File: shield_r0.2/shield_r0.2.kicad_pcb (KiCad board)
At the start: 2 copper layers, 124.5 x 55.9 mm, 10 parts, among them X6 X6, X7 X7, X8 X8, X9 X9

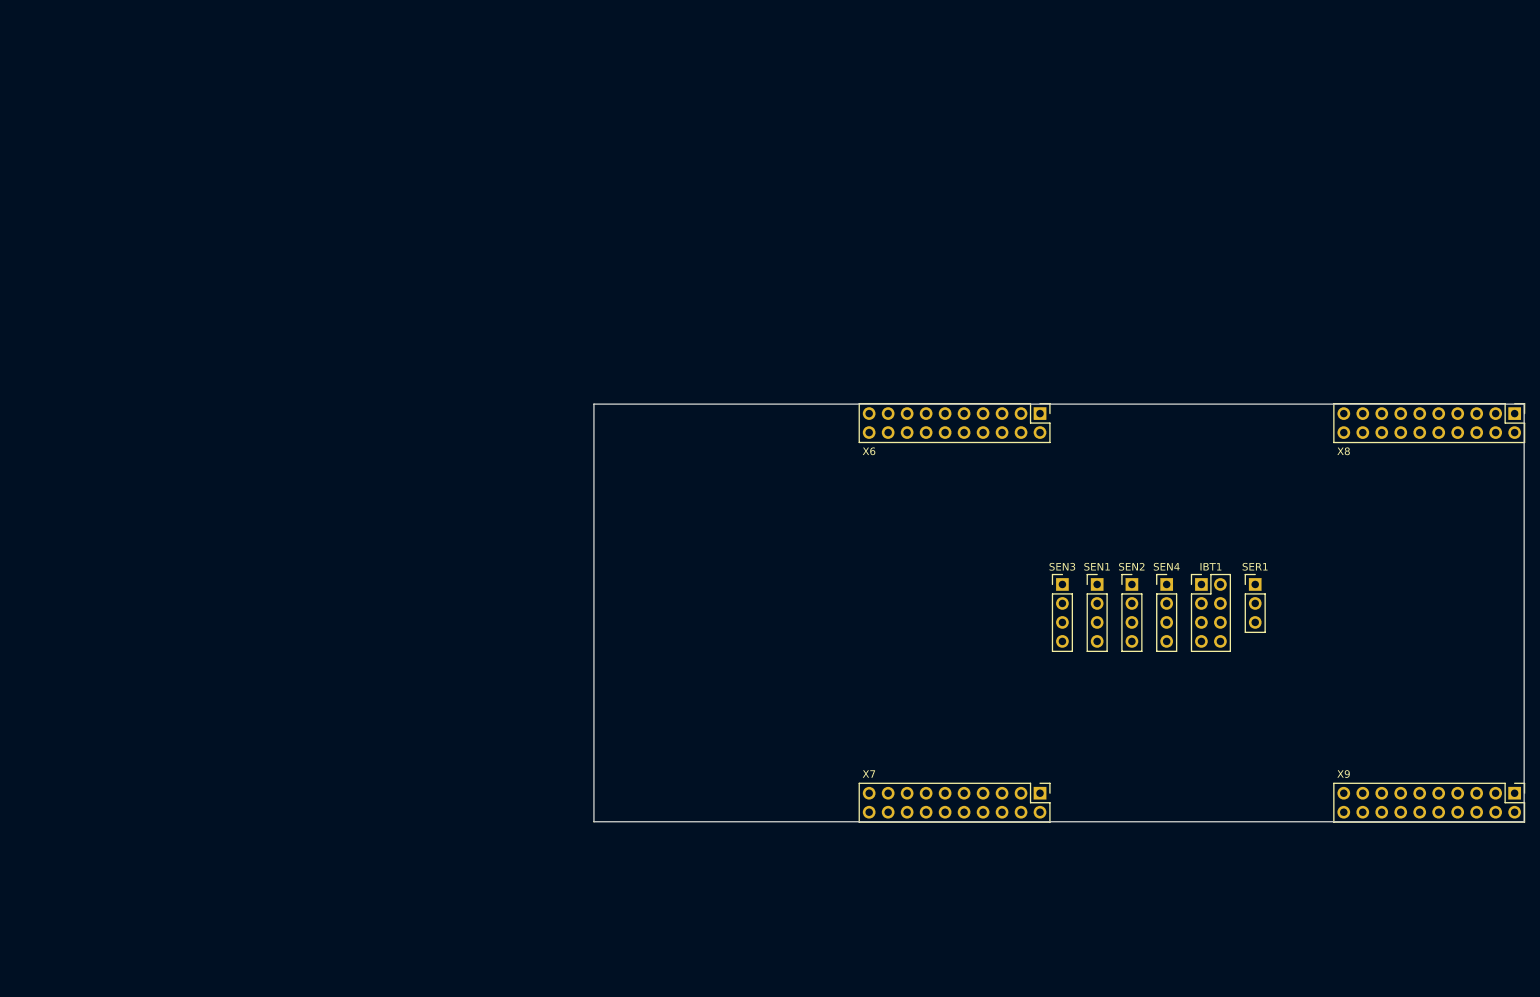
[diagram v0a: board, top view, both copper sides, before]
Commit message: crear librerías ibt-2 y tiva-c, muestra shield
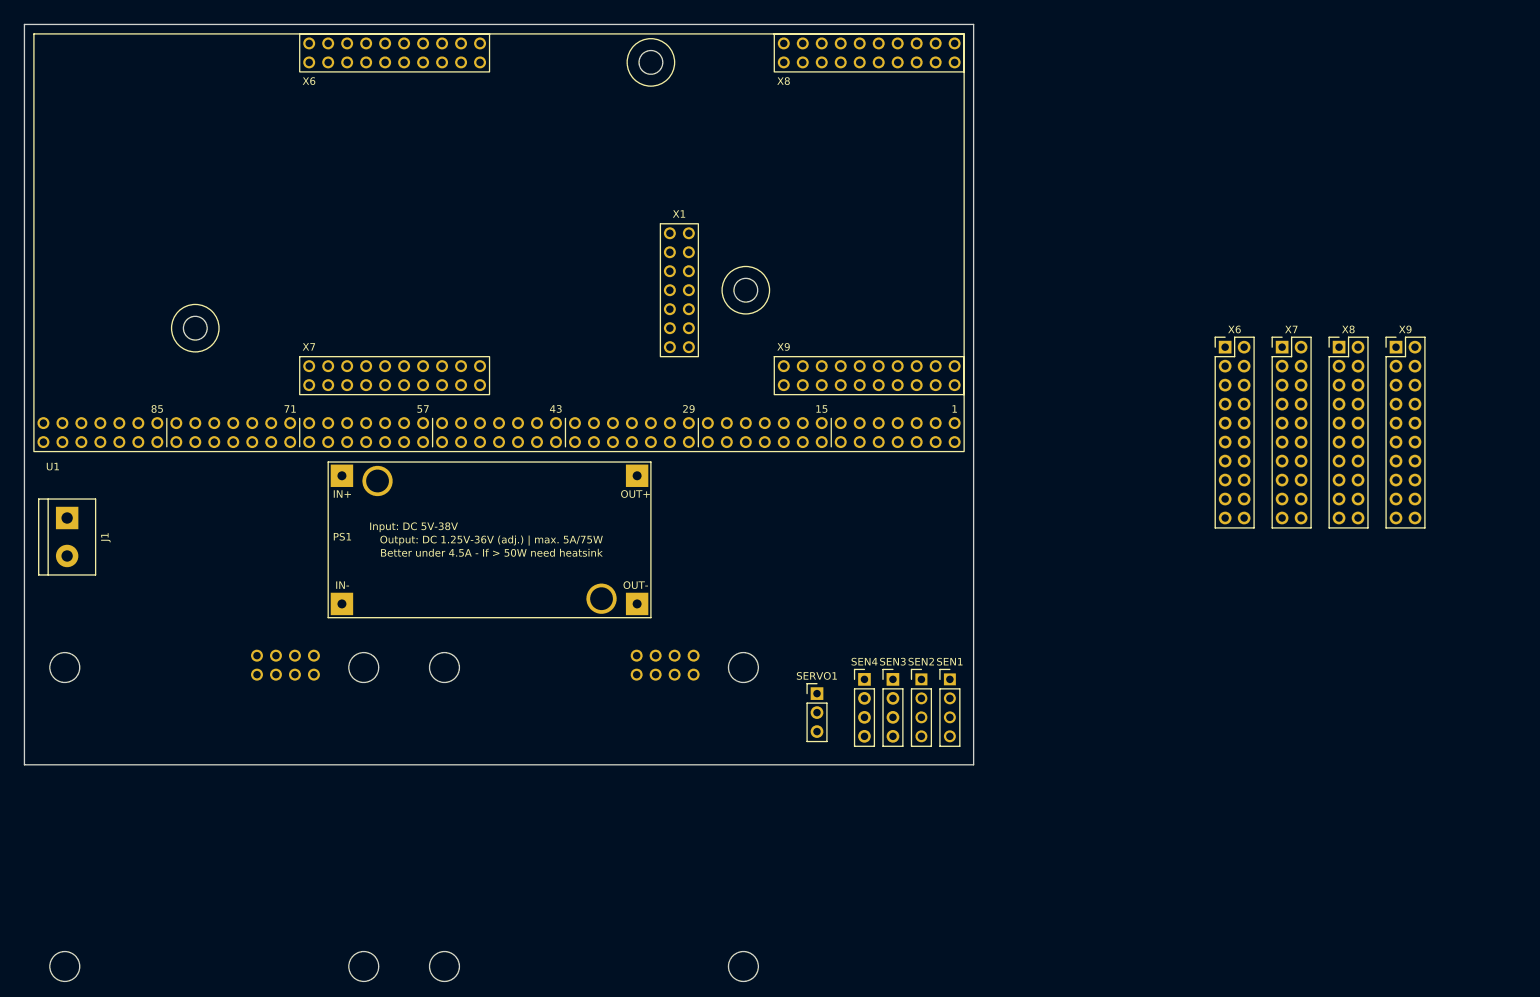
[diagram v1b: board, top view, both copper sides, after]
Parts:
- removed SER1: Conn_01x03, Connector_PinHeader_2.54mm:PinHeader_1x03_P2.54mm_Vertical
- added IBT2: Conn_02x04_Odd_Even, LaunchPad:IBT_2-01, B.Cu at (25.4, 106.0)
- added J1: 12V, TerminalBlock:TerminalBlock_bornier-2_P5.08mm, F.Cu at (5.71, 66.0)
- added PS1: REGULADOR, XL4005:XL4005_DC-DC, F.Cu at (40.6, 79.4)
- added SERVO1: Conn_01x03, Connector_PinHeader_2.54mm:PinHeader_1x03_P2.54mm_Vertical, F.Cu at (106.0, 89.5)
- added U1: EK-TM4C1294XL, LaunchPad:EK-TM4C1294XL-01, F.Cu at (1.27, 57.1)
- IBT1: footprint Connector_PinHeader_2.54mm:PinHeader_2x04_P2.54mm_Vertical -> LaunchPad:IBT_2-01; moved to B.Cu
- moved IBT1 87.0 mm to (76.2, 106.0)
- moved X7 67.9 mm to (168.3, 43.2), turned to 0 degrees
- moved X9 61.8 mm to (183.5, 43.2), turned to 0 degrees
- moved SEN4 42.4 mm to (112.4, 87.6)
- moved SEN2 30.9 mm to (120.0, 87.6)
- moved X6 26.3 mm to (160.7, 43.2), turned to 0 degrees
- moved SEN3 26.0 mm to (116.2, 87.6)
- moved X8 25.1 mm to (175.9, 43.2), turned to 0 degrees
- moved SEN1 23.4 mm to (123.8, 87.6)
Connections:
- net /GND renamed GND
- net /VCC renamed +5V
- IBT1 pad 1: /RPWM -> /RPWM1
- IBT1 pad 2: /LPWM -> /LPWM1
- IBT1 pad 3: /REN -> unconnected-(IBT1-Pin_3-Pad3)
- IBT1 pad 4: /LEN -> unconnected-(IBT1-Pin_4-Pad4)
- IBT1 pad 5: /RIS -> unconnected-(IBT1-Pin_5-Pad5)
- IBT1 pad 6: /LIS -> unconnected-(IBT1-Pin_6-Pad6)
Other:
- board size 124.5 x 55.9 mm -> 127 x 99.1 mm

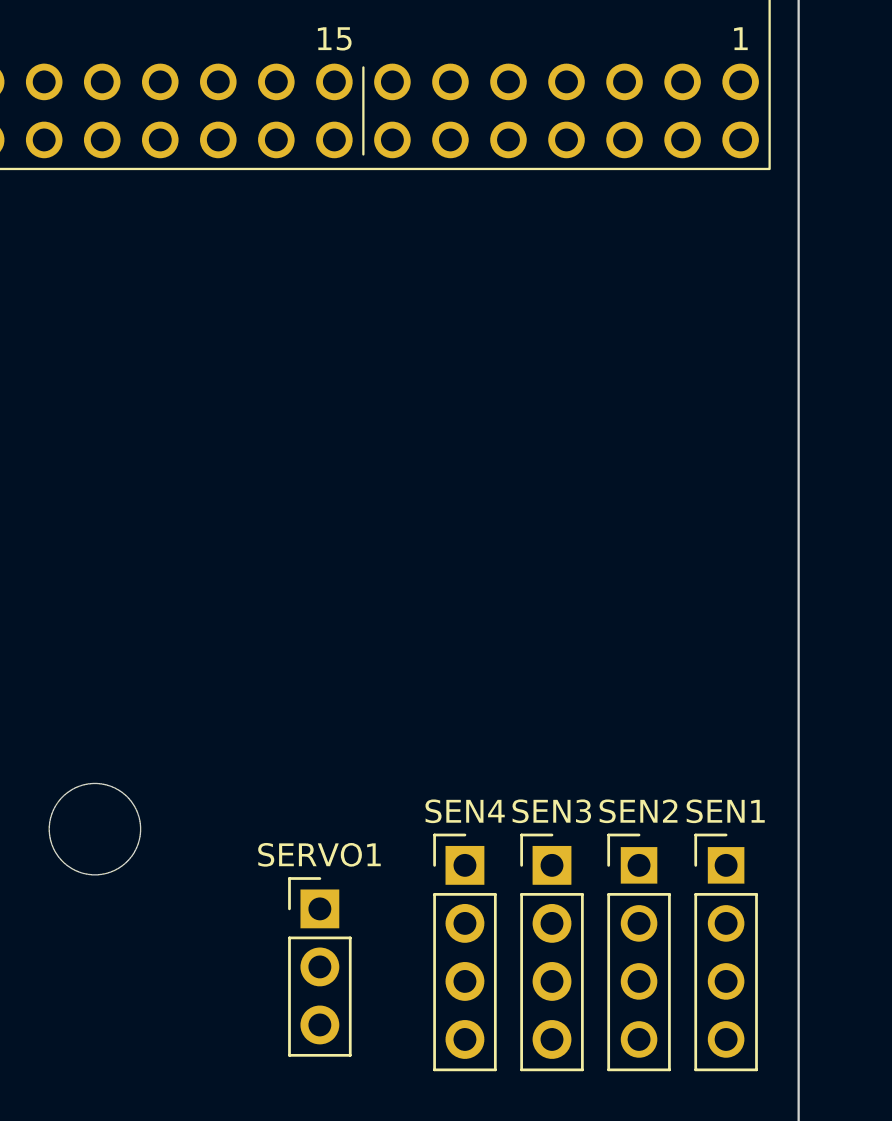
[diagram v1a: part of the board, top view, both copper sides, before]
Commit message: conector bluetooth
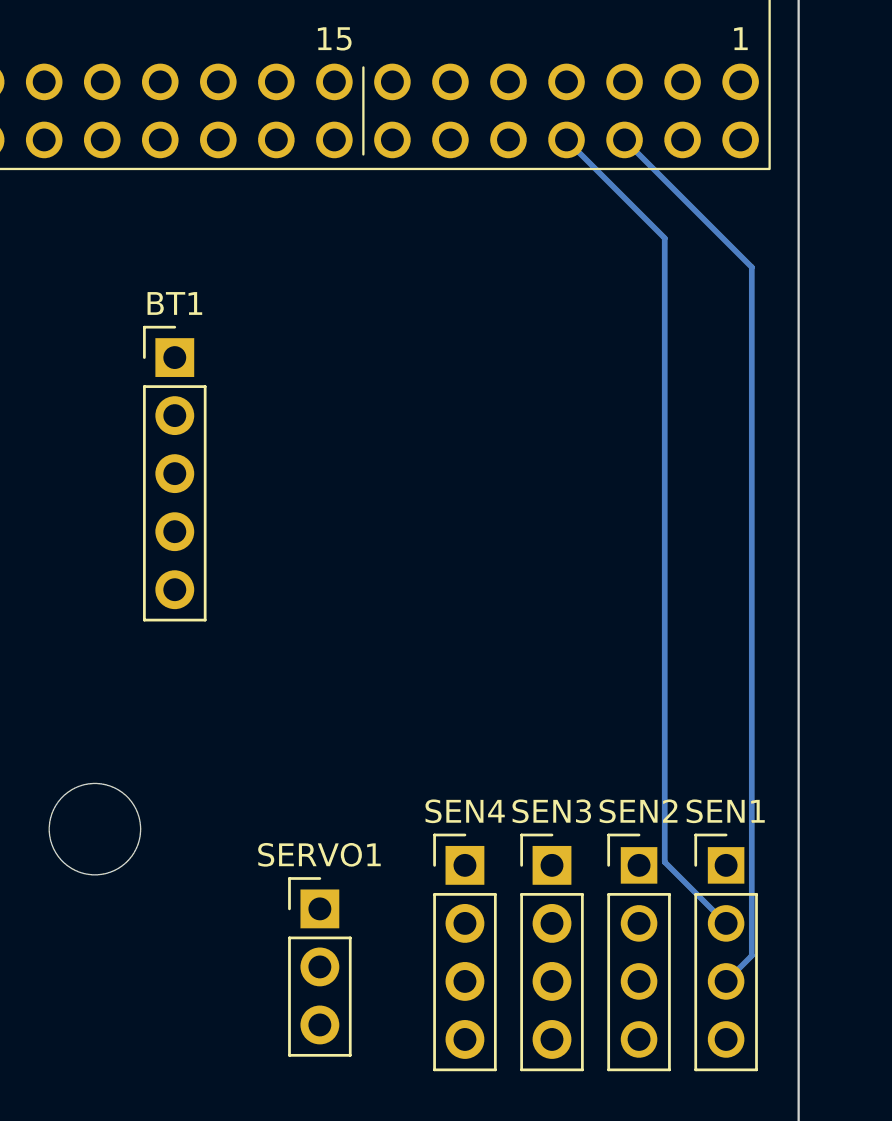
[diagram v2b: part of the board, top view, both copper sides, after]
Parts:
- added BT1: Conn_01x05, Connector_PinHeader_2.54mm:PinHeader_1x05_P2.54mm_Vertical, F.Cu at (99.7, 65.4)
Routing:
- net /ECHO1: track 0.00 -> 39.6 mm
- net /TRIG1: track 0.00 -> 37.2 mm

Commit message: shield para fabricar
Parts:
- removed X6: X6, Connector_PinHeader_2.54mm:PinHeader_2x10_P2.54mm_Vertical
- removed X7: X7, Connector_PinHeader_2.54mm:PinHeader_2x10_P2.54mm_Vertical
- removed X8: X8, Connector_PinHeader_2.54mm:PinHeader_2x10_P2.54mm_Vertical
- removed X9: X9, Connector_PinHeader_2.54mm:PinHeader_2x10_P2.54mm_Vertical
- J1: footprint TerminalBlock:TerminalBlock_bornier-2_P5.08mm -> Connector_Molex:Molex_KK-254_AE-6410-02A_1x02_P2.54mm_Vertical
- PS1: footprint XL4005:XL4005_DC-DC -> Connector_PinHeader_2.54mm:PinHeader_2x02_P2.54mm_Vertical
- moved BT1 64.2 mm to (35.6, 63.5), turned to -90 degrees
- moved PS1 25.0 mm to (55.9, 59.5)
- moved SEN1 21.6 mm to (124.5, 66.0)
- moved SEN2 21.6 mm to (120.7, 66.0)
- moved SEN3 21.6 mm to (116.8, 66.0)
- moved SEN4 21.6 mm to (113.0, 66.0)
- moved SERVO1 21.0 mm to (106.7, 68.6)
- moved IBT1 13.4 mm to (75.6, 92.7)
- moved IBT2 13.4 mm to (24.8, 92.7)
- moved J1 5.12 mm to (5.08, 61.0)
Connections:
- IBT1 pad 3: unconnected-(IBT1-Pin_3-Pad3) -> +5V
- IBT1 pad 4: unconnected-(IBT1-Pin_4-Pad4) -> +5V
- IBT2 pad 3: unconnected-(IBT2-Pin_3-Pad3) -> +5V
- IBT2 pad 4: unconnected-(IBT2-Pin_4-Pad4) -> +5V
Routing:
- net +5V: track 0.00 -> 140.8 mm
- net GND: track 0.00 -> 87.2 mm
- net /RPWM1: track 0.00 -> 57.6 mm
- net /ECHO4: track 0.00 -> 55.8 mm
- net /LPWM1: track 0.00 -> 54.6 mm
- net /TRIG4: track 0.00 -> 52.3 mm
- net +12V: track 0.00 -> 51.8 mm
- net /ECHO3: track 0.00 -> 37.3 mm
- net /TRIG3: track 0.00 -> 34.7 mm
- net /SERVO1: track 0.00 -> 28.1 mm, vias 0 -> 1
- net /TRIG1: track 37.2 -> 15.9 mm
- net /ECHO1: track 39.6 -> 18.4 mm
- net /RPWM2: track 0.00 -> 19.4 mm
- net /ECHO2: track 0.00 -> 18.9 mm
- net /TRIG2: track 0.00 -> 16.4 mm
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- added copper zone on B.Cu, net GND
- added copper zone on F.Cu, net GND
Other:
- board size 127 x 99.1 mm -> 127 x 78.7 mm
